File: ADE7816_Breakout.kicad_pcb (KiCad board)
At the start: 2 copper layers, 66 x 76.2 mm, 56 parts, among them J1 AudioJack3, J2 AudioJack3, J3 AudioJack3, J4 AudioJack3, J5 AudioJack3, J6 AudioJack3, J7 Barrel_Jack_Switch, J8 Conn_01x10, U1 ADE7816ACPZ, Y1 16.384MHz

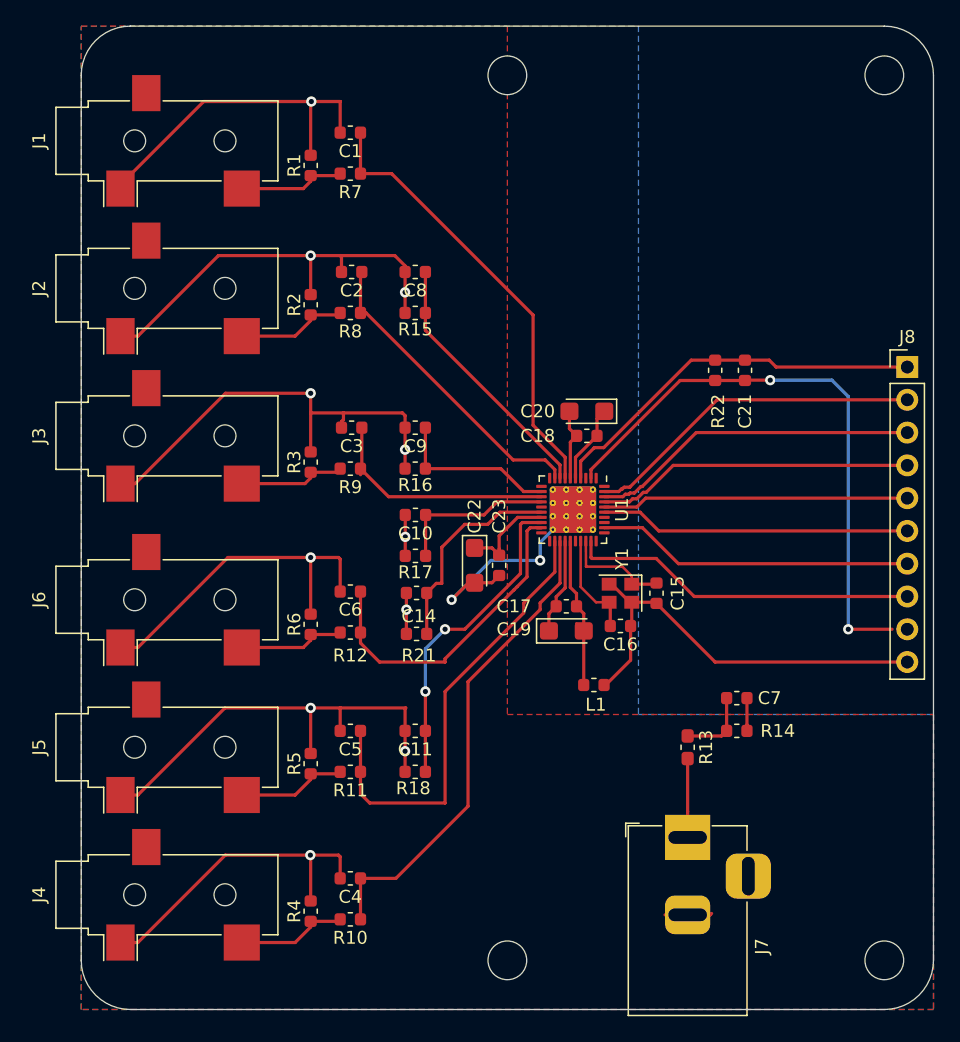
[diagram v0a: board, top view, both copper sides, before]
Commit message: Get some sort of 100% routing with DRC broken
Signed-off-by: Tisham Dhar <whatnickd@gmail.com>
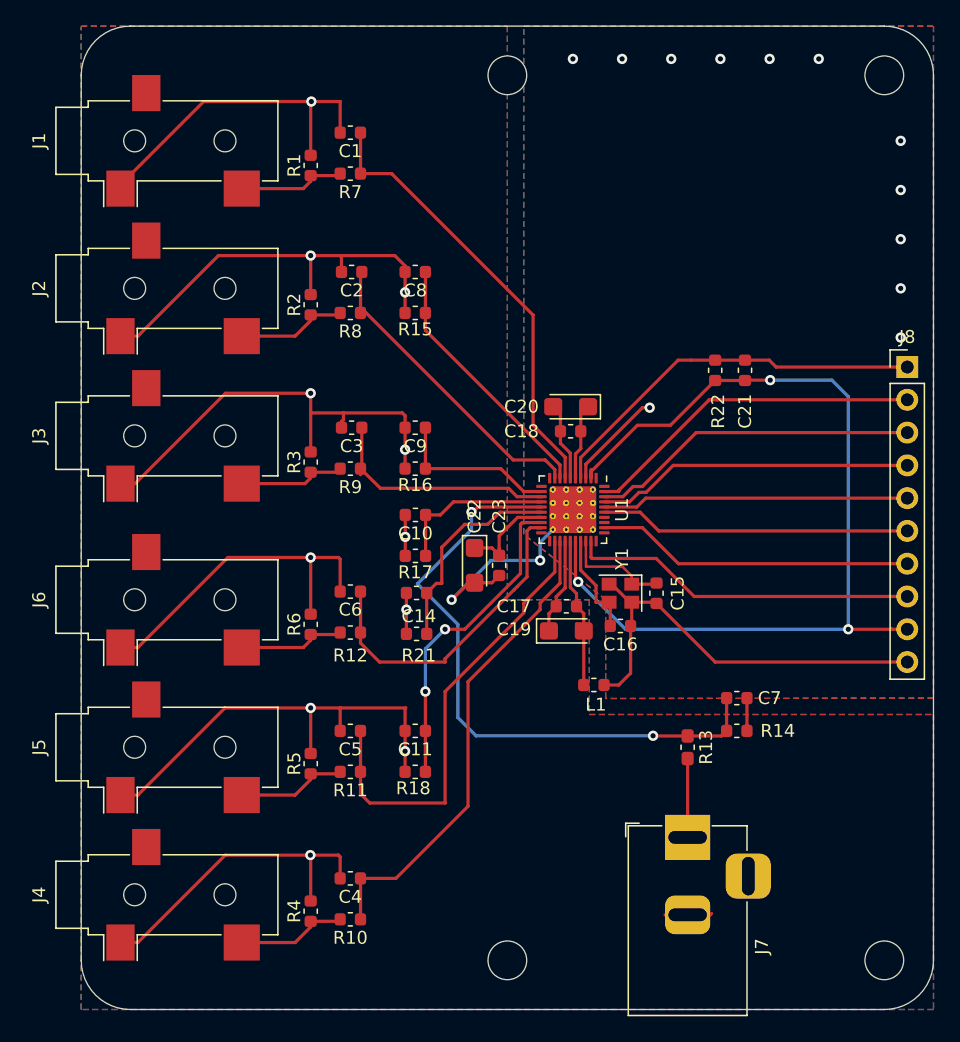
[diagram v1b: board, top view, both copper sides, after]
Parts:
- moved C20 1.31 mm to (131.9, 60.0)
- moved C18 1.31 mm to (131.9, 61.9)
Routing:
- net VP: track 5.73 -> 48.7 mm, vias 0 -> 2
- net +3V3: track 46.2 -> 73.7 mm, vias 2 -> 3
- net GNDD: track 38.6 -> 47.6 mm, vias 0 -> 12
- added copper zone on B.Cu, net GNDD
- added copper zone on F.Cu, net GNDD

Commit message: Add stitching vias
Signed-off-by: Tisham Dhar <whatnickd@gmail.com>
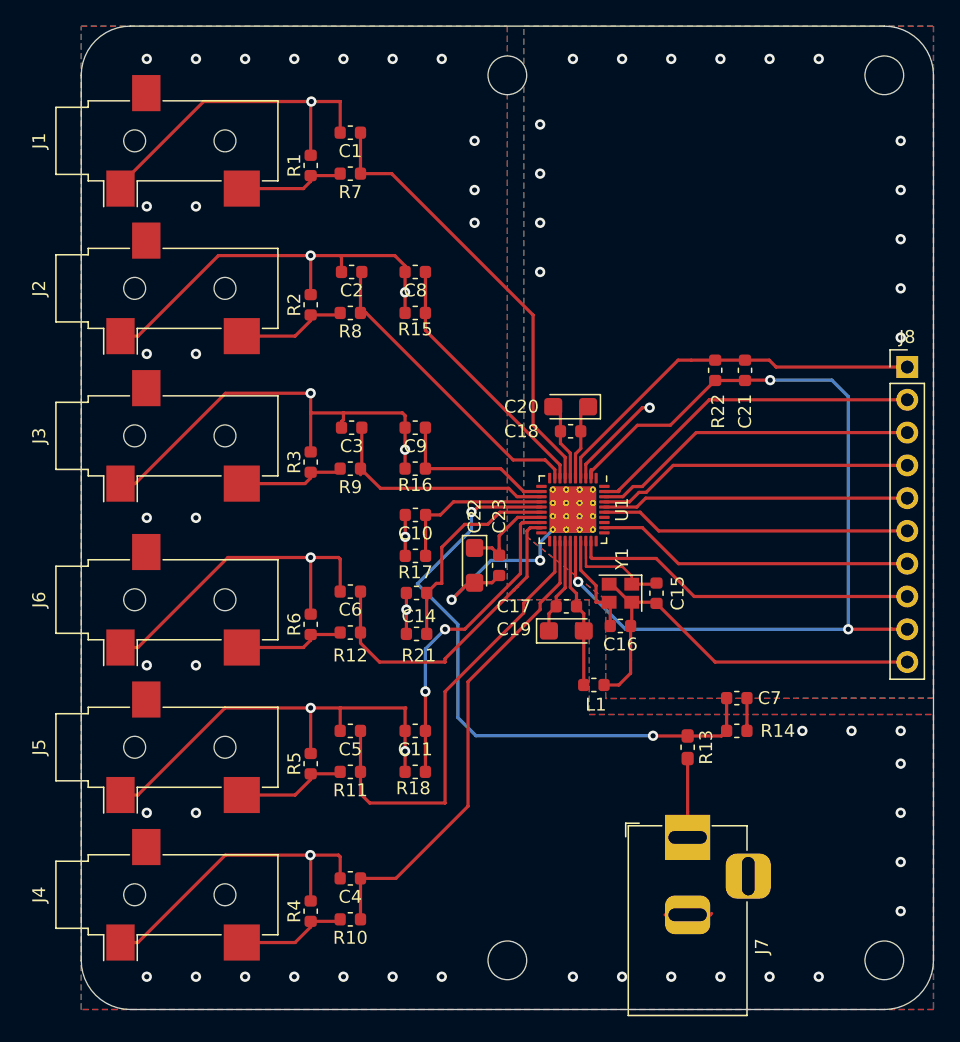
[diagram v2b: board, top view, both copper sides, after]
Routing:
- net GNDD: vias 12 -> 16
- net GNDA: vias 13 -> 53
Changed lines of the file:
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@@
     (thickness 1.6)
     (drawings 10)
-    (tracks 364)
+    (tracks 408)
     (zones 0)
     (modules 56)
@@
   (segment (start 125.73 71.882) (end 122.682 74.93) (width 0.25) (layer B.Cu) (net 6))
   (segment (start 129.54 71.882) (end 125.73 71.882) (width 0.25) (layer B.Cu) (net 6))
+  (via (at 157.48 99.06) (size 0.8) (drill 0.4) (layers F.Cu B.Cu) (net 6))
+  (via (at 157.48 95.25) (size 0.8) (drill 0.4) (layers F.Cu B.Cu) (net 6))
+  (via (at 157.48 91.44) (size 0.8) (drill 0.4) (layers F.Cu B.Cu) (net 6))
+  (via (at 157.48 87.63) (size 0.8) (drill 0.4) (layers F.Cu B.Cu) (net 6))
+  (via (at 151.13 104.14) (size 0.8) (drill 0.4) (layers F.Cu B.Cu) (net 6))
+  (via (at 147.32 104.14) (size 0.8) (drill 0.4) (layers F.Cu B.Cu) (net 6))
+  (via (at 143.51 104.14) (size 0.8) (drill 0.4) (layers F.Cu B.Cu) (net 6))
+  (via (at 139.7 104.14) (size 0.8) (drill 0.4) (layers F.Cu B.Cu) (net 6))
+  (via (at 135.89 104.14) (size 0.8) (drill 0.4) (layers F.Cu B.Cu) (net 6))
+  (via (at 132.08 104.14) (size 0.8) (drill 0.4) (layers F.Cu B.Cu) (net 6))
+  (via (at 121.92 104.14) (size 0.8) (drill 0.4) (layers F.Cu B.Cu) (net 6))
+  (via (at 118.11 104.14) (size 0.8) (drill 0.4) (layers F.Cu B.Cu) (net 6))
+  (via (at 114.3 104.14) (size 0.8) (drill 0.4) (layers F.Cu B.Cu) (net 6))
+  (via (at 110.49 104.14) (size 0.8) (drill 0.4) (layers F.Cu B.Cu) (net 6))
+  (via (at 106.68 104.14) (size 0.8) (drill 0.4) (layers F.Cu B.Cu) (net 6))
+  (via (at 102.87 104.14) (size 0.8) (drill 0.4) (layers F.Cu B.Cu) (net 6))
+  (via (at 99.06 104.14) (size 0.8) (drill 0.4) (layers F.Cu B.Cu) (net 6))
+  (via (at 99.06 91.44) (size 0.8) (drill 0.4) (layers F.Cu B.Cu) (net 6))
+  (via (at 102.87 91.44) (size 0.8) (drill 0.4) (layers F.Cu B.Cu) (net 6))
+  (via (at 99.06 80.01) (size 0.8) (drill 0.4) (layers F.Cu B.Cu) (net 6))
+  (via (at 102.87 80.01) (size 0.8) (drill 0.4) (layers F.Cu B.Cu) (net 6))
+  (via (at 99.06 68.58) (size 0.8) (drill 0.4) (layers F.Cu B.Cu) (net 6))
+  (via (at 102.87 68.58) (size 0.8) (drill 0.4) (layers F.Cu B.Cu) (net 6))
+  (via (at 99.06 55.88) (size 0.8) (drill 0.4) (layers F.Cu B.Cu) (net 6))
+  (via (at 102.87 55.88) (size 0.8) (drill 0.4) (layers F.Cu B.Cu) (net 6))
+  (via (at 121.92 33.02) (size 0.8) (drill 0.4) (layers F.Cu B.Cu) (net 6))
+  (via (at 118.11 33.02) (size 0.8) (drill 0.4) (layers F.Cu B.Cu) (net 6))
+  (via (at 114.3 33.02) (size 0.8) (drill 0.4) (layers F.Cu B.Cu) (net 6))
+  (via (at 110.49 33.02) (size 0.8) (drill 0.4) (layers F.Cu B.Cu) (net 6))
+  (via (at 106.68 33.02) (size 0.8) (drill 0.4) (layers F.Cu B.Cu) (net 6))
+  (via (at 102.87 33.02) (size 0.8) (drill 0.4) (layers F.Cu B.Cu) (net 6))
+  (via (at 99.06 33.02) (size 0.8) (drill 0.4) (layers F.Cu B.Cu) (net 6))
+  (via (at 124.46 39.37) (size 0.8) (drill 0.4) (layers F.Cu B.Cu) (net 6))
+  (via (at 124.46 43.18) (size 0.8) (drill 0.4) (layers F.Cu B.Cu) (net 6))
+  (via (at 124.46 45.72) (size 0.8) (drill 0.4) (layers F.Cu B.Cu) (net 6))
+  (via (at 157.48 85.09) (size 0.8) (drill 0.4) (layers F.Cu B.Cu) (net 6))
+  (via (at 153.67 85.09) (size 0.8) (drill 0.4) (layers F.Cu B.Cu) (net 6))
+  (via (at 149.86 85.09) (size 0.8) (drill 0.4) (layers F.Cu B.Cu) (net 6))
+  (via (at 99.06 44.45) (size 0.8) (drill 0.4) (layers F.Cu B.Cu) (net 6))
+  (via (at 102.87 44.45) (size 0.8) (drill 0.4) (layers F.Cu B.Cu) (net 6))
   (segment (start 111.76 42.5) (end 111.76 42.0625) (width 0.25) (layer F.Cu) (net 7))
   (segment (start 111.19 43.07) (end 111.76 42.5) (width 0.25) (layer F.Cu) (net 7))
@@
   (segment (start 136.5505 80.6195) (end 136.5505 79.6035) (width 0.25) (layer F.Cu) (net 9))
   (segment (start 135.636 81.534) (end 136.5505 80.6195) (width 0.25) (layer F.Cu) (net 9))
+  (via (at 129.54 38.1) (size 0.8) (drill 0.4) (layers F.Cu B.Cu) (net 9))
+  (via (at 129.54 41.91) (size 0.8) (drill 0.4) (layers F.Cu B.Cu) (net 9))
+  (via (at 129.54 45.72) (size 0.8) (drill 0.4) (layers F.Cu B.Cu) (net 9))
+  (via (at 129.54 49.53) (size 0.8) (drill 0.4) (layers F.Cu B.Cu) (net 9))
   (segment (start 134.9755 75.2095) (end 134.888 75.122) (width 0.25) (layer F.Cu) (net 27))
   (segment (start 134.9755 76.962) (end 134.9755 75.2095) (width 0.25) (layer F.Cu) (net 27))

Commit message: Modified the library symbols used for the stereo jack and DC jack. Made stereo jack footprint reference local copy in folder lib/misc.pretty to avoid compatibility issues between different versions of the system component libraries. Rerouted the board using 0.2mm tracks and 0.15mm spacing and 0.3mm drill vias. and changed the ground plane patterns to be nicer.
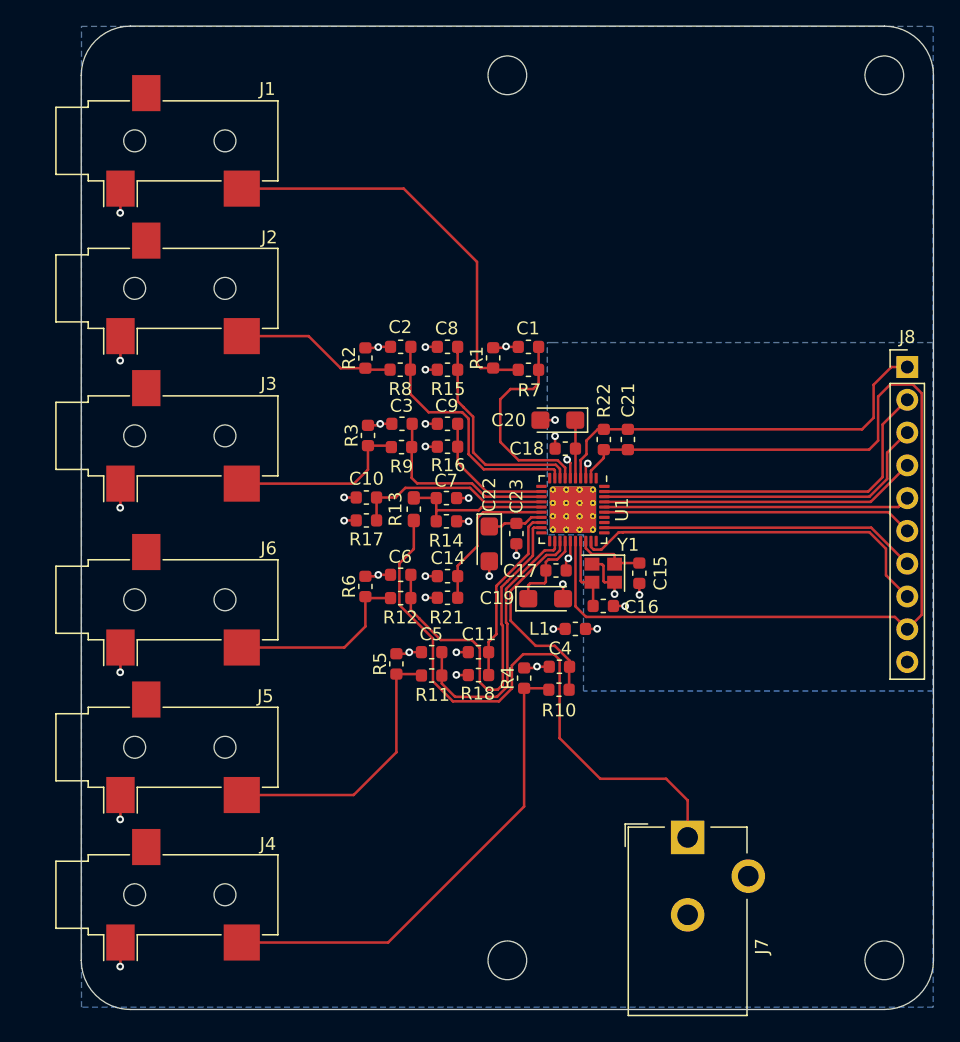
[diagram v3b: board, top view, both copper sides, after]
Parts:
- J1, J2, J3, J4, J5, J6: footprint Connector_Audio:Jack_3.5mm_CUI_SJ-3523-SMT_Horizontal -> misc:Jack_3.5mm_CUI_SJ-3523-SMT_Horizontal
- J7: footprint Connector_BarrelJack:BarrelJack_Horizontal -> Connectors:Barrel_Jack_CUI_PJ-102AH
- moved R13 28.1 mm to (119.8, 67.9)
- moved R14 27.7 mm to (122.3, 68.8)
- moved C7 27.3 mm to (122.3, 67.0)
- moved R4 24.5 mm to (128.3, 81.0)
- moved R10 24.0 mm to (131.0, 81.9)
- moved C4 23.1 mm to (131.0, 80.1)
- moved C1 21.6 mm to (128.6, 55.3)
- moved R1 20.6 mm to (125.9, 56.2)
- moved R7 20.5 mm to (128.6, 57.1)
- moved C21 10.5 mm to (136.3, 62.5)
- moved R5 10.2 mm to (118.4, 79.9)
- moved R22 10.2 mm to (134.5, 62.5)
- moved R11 9.77 mm to (121.1, 80.8)
- moved R18 8.96 mm to (124.8, 80.8)
- moved C5 8.77 mm to (121.1, 79.0)
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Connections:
- J7 pad 3: Net-(J7-Pad3) -> (no net)
- R1 pad 2: Net-(J1-PadT) -> Net-(J1-Pad2)
- R10 pad 2: Net-(J4-PadT) -> Net-(J4-Pad2)
- R11 pad 2: Net-(J5-PadT) -> Net-(J5-Pad2)
- R12 pad 2: Net-(J6-PadT) -> Net-(J6-Pad2)
- R2 pad 2: Net-(J2-PadT) -> Net-(J2-Pad2)
- R3 pad 2: Net-(J3-PadT) -> Net-(J3-Pad2)
- R4 pad 2: Net-(J4-PadT) -> Net-(J4-Pad2)
- R5 pad 2: Net-(J5-PadT) -> Net-(J5-Pad2)
- R6 pad 2: Net-(J6-PadT) -> Net-(J6-Pad2)
- R7 pad 2: Net-(J1-PadT) -> Net-(J1-Pad2)
- R8 pad 2: Net-(J2-PadT) -> Net-(J2-Pad2)
- R9 pad 2: Net-(J3-PadT) -> Net-(J3-Pad2)
- U1 pad 1: Net-(U1-Pad1) -> (no net)
- U1 pad 10: Net-(U1-Pad10) -> (no net)
- U1 pad 11: Net-(U1-Pad11) -> (no net)
- U1 pad 20: Net-(U1-Pad20) -> (no net)
- U1 pad 21: Net-(U1-Pad21) -> (no net)
- U1 pad 30: Net-(U1-Pad30) -> (no net)
- U1 pad 31: Net-(U1-Pad31) -> (no net)
- U1 pad 33: Net-(U1-Pad33) -> (no net)
- U1 pad 34: Net-(U1-Pad34) -> (no net)
- U1 pad 40: Net-(U1-Pad40) -> (no net)
- U1 pad 41: GNDA -> GNDD
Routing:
- net GNDA: track 224.2 -> 41.0 mm, vias 53 -> 29
- net Net-(J7-Pad1): track 6.11 -> 48.1 mm
- net Net-(J4-Pad2): track 0.00 -> 37.4 mm
- net VP: track 48.7 -> 11.8 mm, vias 2 -> 0
- net GNDD: track 47.6 -> 11.5 mm, vias 16 -> 8
- net Net-(J1-Pad2): track 0.00 -> 31.9 mm
- net Net-(J5-Pad2): track 0.00 -> 21.4 mm
- net IDP: track 37.3 -> 16.3 mm
- net IAP: track 34.8 -> 16.3 mm
- net Net-(J6-Pad2): track 0.00 -> 14.6 mm
- net IEP: track 35.5 -> 21.5 mm
- net Net-(J3-Pad2): track 0.00 -> 13.9 mm
- net Net-(J2-Pad2): track 0.00 -> 12.6 mm
- net IN: track 24.8 -> 13.9 mm, vias 2 -> 0
- net Net-(J5-PadT): track 8.63 -> 0.00 mm
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- removed copper zone on F.Cu, net GNDA
- removed copper zone on F.Cu, net GNDD
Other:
- net class Default: clearance 0.2 -> 0.15; trace_width 0.25 -> 0.2; via_dia 0.8 -> 0.6; via_drill 0.4 -> 0.3
- rule trace_clearance: 0.2 -> 0.15

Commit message: Merge routing and fix footprint
Signed-off-by: Tisham Dhar <whatnickd@gmail.com>
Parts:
- R13: footprint Resistor_SMD:R_0603_1608Metric_Pad1.05x0.95mm_HandSolder -> Resistor_SMD:R_0603_1608Metric
- U1: footprint Package_DFN_QFN:QFN-40-1EP_5x5mm_P0.4mm_EP3.6x3.6mm_ThermalVias -> Package_DFN_QFN:QFN-40-1EP_6x6mm_P0.5mm_EP4.6x4.6mm_ThermalVias
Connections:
- J1 pad 3: (no net) -> Net-(J1-Pad3)
- J2 pad 3: (no net) -> Net-(J2-Pad3)
- J3 pad 3: (no net) -> Net-(J3-Pad3)
- J4 pad 3: (no net) -> Net-(J4-Pad3)
- J5 pad 3: (no net) -> Net-(J5-Pad3)
- J6 pad 3: (no net) -> Net-(J6-Pad3)
- J7 pad 3: (no net) -> Net-(J7-Pad3)
- U1 pad 1: (no net) -> Net-(U1-Pad1)
- U1 pad 10: (no net) -> Net-(U1-Pad10)
- U1 pad 11: (no net) -> Net-(U1-Pad11)
- U1 pad 20: (no net) -> Net-(U1-Pad20)
- U1 pad 21: (no net) -> Net-(U1-Pad21)
- U1 pad 30: (no net) -> Net-(U1-Pad30)
- U1 pad 31: (no net) -> Net-(U1-Pad31)
- U1 pad 33: (no net) -> Net-(U1-Pad33)
- U1 pad 34: (no net) -> Net-(U1-Pad34)
- U1 pad 40: (no net) -> Net-(U1-Pad40)
